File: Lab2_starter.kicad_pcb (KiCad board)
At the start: 4 copper layers, 121.8 x 101.6 mm, 77 parts, among them J1 973582101, J10 Conn_01x02, J11 Conn_01x02, J12 Conn_01x02, J13 Conn_01x02, J14 Conn_01x02, J15 Conn_01x02, J16 Conn_01x02, J2 973582100, J3 973582101, J4 973582100, J5 Conn_01x01, J6 Conn_01x01, J7 Conn_01x02, J8 Conn_01x02, J9 Conn_01x02, Q1 NMOS, Q2 NMOS, SW1 SW_Push_DPDT, U1 IR2010, U2 CT416-HSN820DR, U3 LAUNCHXL-F28P55X_BottomHalf

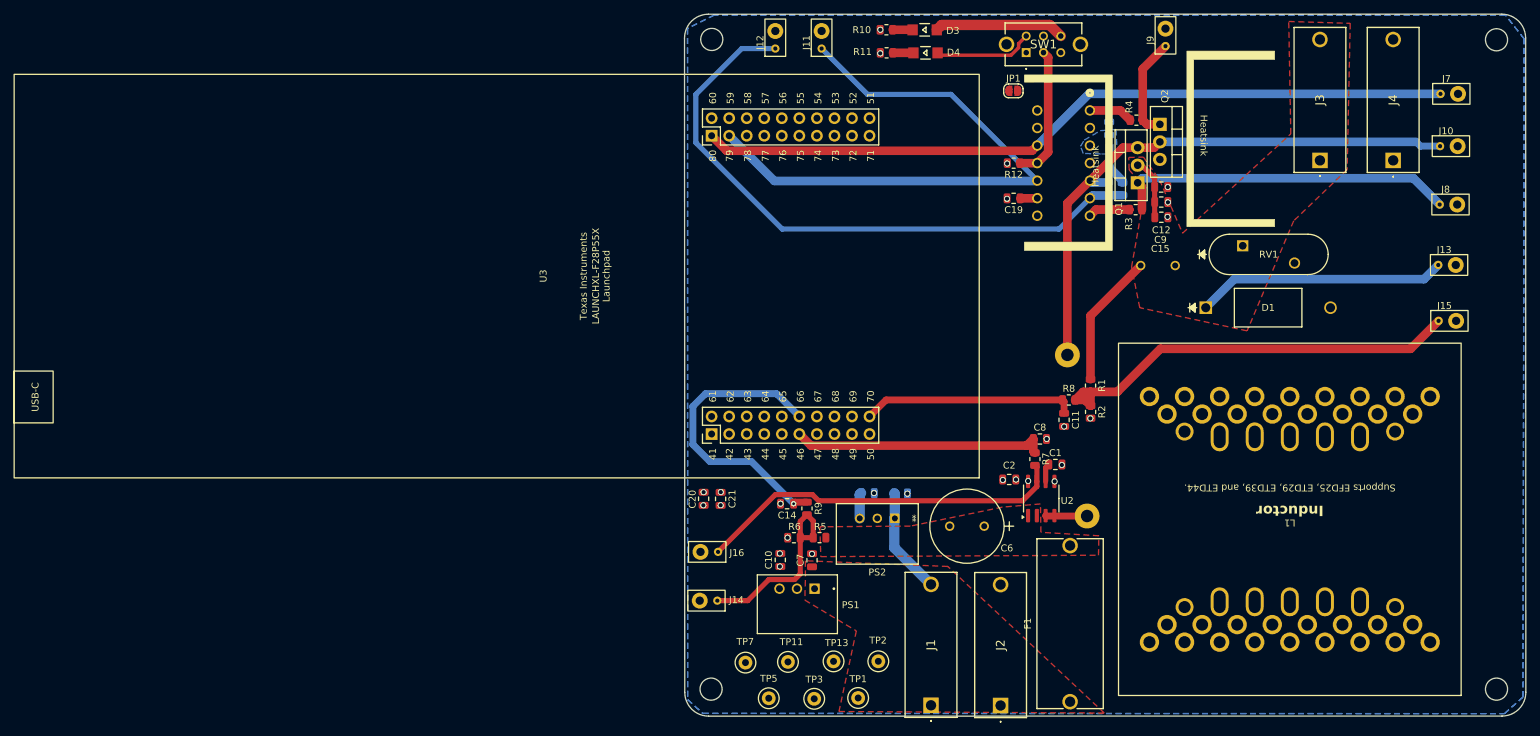
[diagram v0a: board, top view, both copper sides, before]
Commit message: Fix high didt pathways
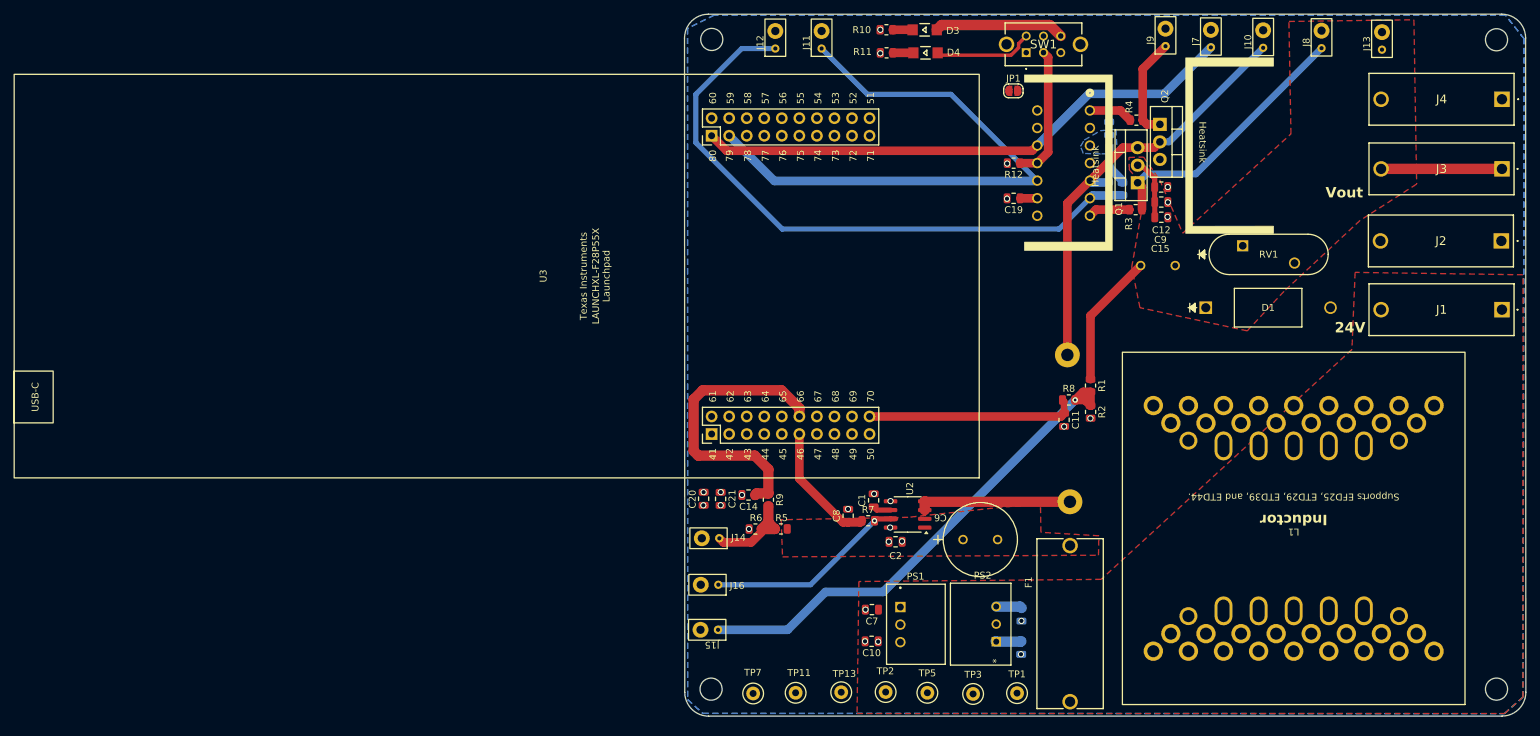
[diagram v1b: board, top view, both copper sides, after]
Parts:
- moved J15 115.8 mm to (23.6, 127.0), turned to 180 degrees
- moved J1 100.6 mm to (138.4, 80.7), turned to 180 degrees
- moved J2 98.9 mm to (138.3, 70.7), turned to 180 degrees
- moved J7 35.4 mm to (96.2, 41.4), turned to 90 degrees
- moved J13 33.8 mm to (121.0, 41.8), turned to 90 degrees
- moved J10 31.0 mm to (103.8, 41.5), turned to 90 degrees
- moved J8 30.1 mm to (112.3, 41.5), turned to 90 degrees
- moved C8 29.9 mm to (43.7, 110.5), turned to 90 degrees
- moved C17 28.4 mm to (68.8, 124.8), turned to -90 degrees
- moved C13 28.3 mm to (68.8, 129.6), turned to -90 degrees
- moved C1 26.8 mm to (47.4, 108.3), turned to 90 degrees
- moved J3 26.4 mm to (138.4, 60.3), turned to 180 degrees
- moved R7 25.7 mm to (46.6, 111.2), turned to 0 degrees
- moved PS2 23.1 mm to (65.2, 128.7), turned to 90 degrees
- moved TP1 23.0 mm to (68.2, 136.2)
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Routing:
- net C2000 D : track 109.8 -> 79.4 mm
- net I_L: track 54.0 -> 29.6 mm, vias 0 -> 1
- net Vsw: track 82.6 -> 62.4 mm
- net /ADCINA9: track 37.1 -> 18.2 mm
- net Vout: track 64.8 -> 46.1 mm
- net Net-(J6-Pin_1): track 6.02 -> 22.3 mm
- net Vin_sens: track 28.1 -> 14.4 mm
- net +24V: track 15.4 -> 3.75 mm
- net D': track 49.7 -> 38.8 mm
- net Vout_sens: track 61.9 -> 72.8 mm, vias 0 -> 1
- net /ADCINA0: track 30.9 -> 30.4 mm
- net /ADCINA4: track 43.2 -> 43.0 mm, vias 1 -> 0
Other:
- board text added: "24V"
- board text added: "Vout"

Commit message: Silk Screen
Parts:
- C13, C17: moved to F.Cu
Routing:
- net +24V: track 3.75 -> 0.00 mm
- net I_L: track 29.6 -> 28.9 mm

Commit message: Fixed ADC
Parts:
- C1, C10, C13, C14, C17, C2, C7, C8, R5, R6, R7, R9, U2: moved to B.Cu
- C4: moved to F.Cu
- moved J15 135.5 mm to (129.0, 41.9), turned to 90 degrees
- moved R6 23.3 mm to (39.6, 91.0)
- moved R5 21.6 mm to (43.5, 92.9)
- moved C14 16.9 mm to (36.8, 92.3), turned to 90 degrees
- moved R9 16.8 mm to (39.7, 93.1), turned to 0 degrees
- moved C2 15.5 mm to (49.3, 98.8), turned to 90 degrees
- moved J6 13.9 mm to (77.4, 94.7)
- moved U2 13.0 mm to (53.1, 97.3), turned to -90 degrees
- moved C8 11.9 mm to (35.8, 101.6), turned to 180 degrees
- moved C11 11.5 mm to (77.3, 85.4)
- moved R1 11.5 mm to (81.2, 80.4)
- moved R2 11.5 mm to (81.2, 84.2)
- moved R8 11.5 mm to (78.0, 82.5)
- moved J5 11.3 mm to (75.5, 76.0)
- moved R7 10.2 mm to (51.4, 102.1)
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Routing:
- net /ADCINA4: track 43.0 -> 4.93 mm
- net Vin_sens: track 14.4 -> 46.3 mm
- net Vout: track 46.1 -> 20.4 mm
- net GND: track 0.00 -> 17.1 mm, vias 21 -> 15
- net I_L: track 28.9 -> 38.2 mm, vias 1 -> 0
- net Vin: track 0.00 -> 8.90 mm, vias 0 -> 1
- net Vsw: track 62.4 -> 54.4 mm
- net /ADCINA0: track 30.4 -> 37.4 mm
- net +3.3V: track 2.48 -> 6.26 mm, vias 6 -> 4
- net +24V: track 0.00 -> 3.65 mm
- net D: track 14.8 -> 17.7 mm
- net /ADCINA9: track 18.2 -> 16.9 mm
- net Net-(J6-Pin_1): track 22.3 -> 23.6 mm
- net Vout_sens: track 72.8 -> 73.7 mm

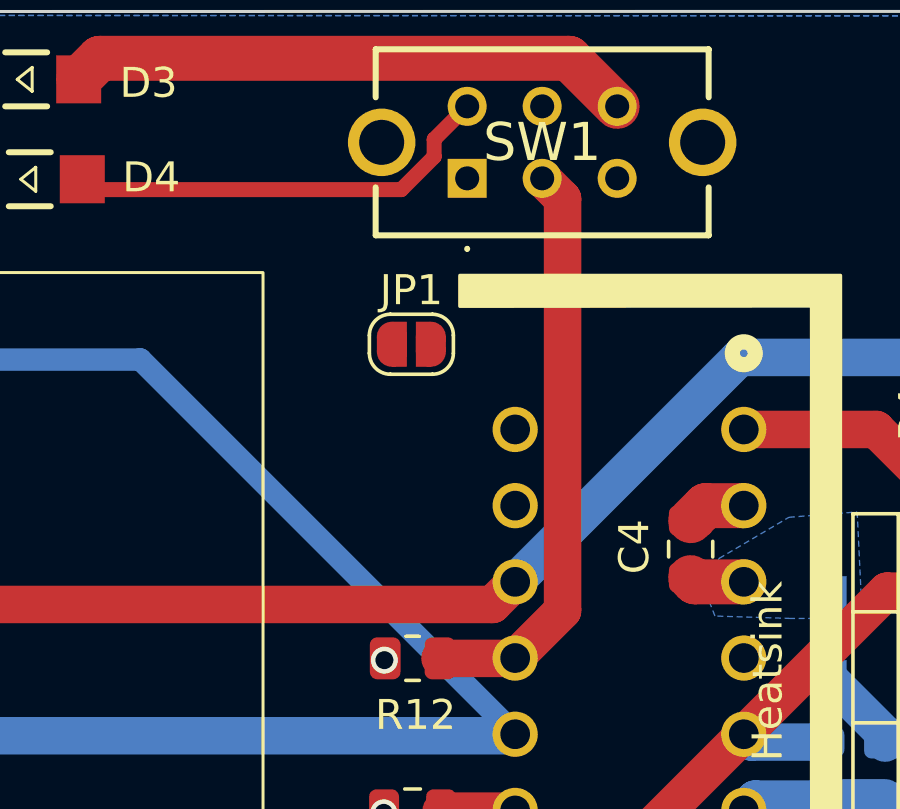
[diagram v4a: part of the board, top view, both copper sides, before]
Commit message: Fixed filled zones
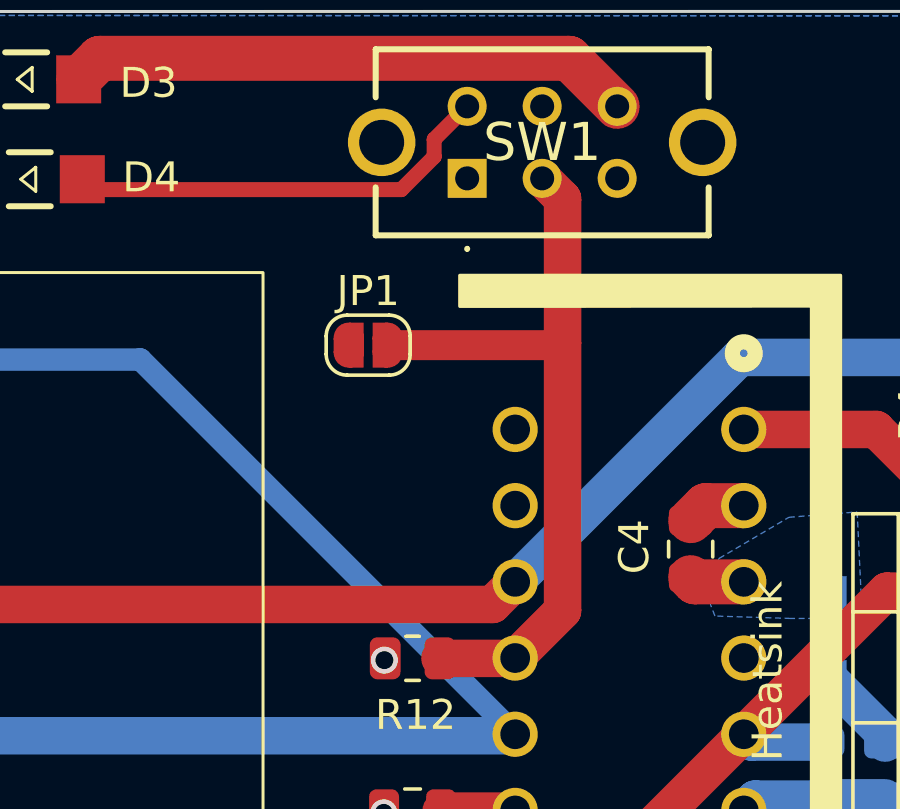
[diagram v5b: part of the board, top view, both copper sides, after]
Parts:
- moved JP1 1.44 mm to (66.2, 49.0)
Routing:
- net SD: track 19.4 -> 25.3 mm
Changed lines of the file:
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@@
 	(footprint "Jumper:SolderJumper-2_P1.3mm_Open_RoundedPad1.0x1.5mm"
 		(layer "F.Cu")
-		(at 67.66 48.99)
+		(at 66.22 49.02)
 		(descr "SMD Solder Jumper, 1x1.5mm, rounded Pads, 0.3mm gap, open")
 		(tags "solder jumper open")
@@
 	)
 	(segment
+		(start 72.629999 49.02)
+		(end 72.699999 48.95)
+		(width 1)
+		(layer "F.Cu")
+		(net 27)
+	)
+	(segment
+		(start 72.699999 48.95)
+		(end 72.699999 44.139999)
+		(width 1.25)
+		(layer "F.Cu")
+		(net 27)
+	)
+	(segment
+		(start 66.87 49.02)
+		(end 72.629999 49.02)
+		(width 1)
+		(layer "F.Cu")
+		(net 27)
+	)
+	(segment
 		(start 71.11 59.46)
 		(end 71.12 59.45)
@@
 	(segment
 		(start 72.699999 57.870001)
-		(end 72.699999 44.139999)
+		(end 72.699999 48.95)
 		(width 1.25)
 		(layer "F.Cu")
@@
 		(layer "F.Cu")
 		(hatch edge 0.5)
-		(connect_pads
+		(connect_pads yes
 			(clearance 0.5)
 		)
@@
 		(hatch edge 0.5)
 		(priority 3)
-		(connect_pads
+		(connect_pads yes
 			(clearance 0.5)
 		)
@@
 		(hatch edge 0.5)
 		(priority 2)
-		(connect_pads
+		(connect_pads yes
 			(clearance 0.5)
 		)
@@
 		(hatch edge 0.5)
 		(priority 10)
-		(connect_pads
+		(connect_pads yes
 			(clearance 0.5)
 		)
@@
 		(hatch edge 0.5)
 		(priority 7)
-		(connect_pads
+		(connect_pads yes
 			(clearance 0.5)
 		)
@@
 		(hatch edge 0.5)
 		(priority 8)
-		(connect_pads
+		(connect_pads yes
 			(clearance 0.5)
 		)
